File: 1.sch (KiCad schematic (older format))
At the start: 44 parts, among them J1 Micro_SD_Card, J10 I2C1, J11 I2C2, J12 B3..9A, J2 USB_B_Micro, J3 Conn_Power, J4 SWD, J5 Protected, J6 SPI1, J7 ADC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

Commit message: SD ground
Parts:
- J1: symbol Connector:Micro_SD_Card -> Connector:Micro_SD_Card_Det
- Y2: symbol Device:Crystal -> Device:Crystal_GND3
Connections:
- net GND: now also J1.10 (DET_A), J1.11 (SHIELD), Y2.3
- net OSC_32K1: now also Y2.1; no longer Y2.2
- net OSC_32K2: now also Y2.2; no longer Y2.1
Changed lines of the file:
@@
 Connection ~ 1000 2300
 Wire Wire Line
-	1000 2300 1000 2700
+	1000 2300 1000 2500
 Wire Wire Line
 	1250 2700 1000 2700
@@
 	1    8350 1250
 	1    0    0    -1
-$EndComp
-$Comp
-L Connector:Micro_SD_Card J1
-U 1 1 60953440
-P 1600 6700
-F 0 "J1" H 1550 7417 50  0000 C CNN
-F 1 "Micro_SD_Card" H 1550 7326 50  0000 C CNN
-F 2 "Connector_Card:microSD_HC_Hirose_DM3BT-DSF-PEJS" H 2750 7000 50  0001 C CNN
-F 3 "http://katalog.we-online.de/em/datasheet/693072010801.pdf" H 1600 6700 50  0001 C CNN
-	1    1600 6700
-	-1   0    0    -1
 $EndComp
 Wire Wire Line
@@
 Wire Wire Line
 	5450 2850 5550 2850
-Wire Wire Line
-	2600 6900 2600 7450
 Connection ~ 2600 7450
 Wire Wire Line
 	2600 7450 2600 7550
-Wire Wire Line
-	800  7300 800  7450
 Wire Wire Line
 	800  7450 2600 7450
@@
 	1750 2700 1900 2700
 $Comp
-L Device:Crystal Y2
-U 1 1 60880457
-P 1900 2500
-F 0 "Y2" V 1946 2369 50  0000 R CNN
-F 1 "32.768k" V 1855 2369 50  0000 R CNN
-F 2 "Crystal:Crystal_DS26_D2.0mm_L6.0mm_Horizontal_1EP_style1" H 1900 2500 50  0001 C CNN
-F 3 "~" H 1900 2500 50  0001 C CNN
-	1    1900 2500
-	0    -1   -1   0
-$EndComp
-$Comp
 L Connector_Generic:Conn_01x06 J10
 U 1 1 6153F296
@@
 	9300 1250 9200 1250
 Connection ~ 9200 1250
+$Comp
+L Connector:Micro_SD_Card_Det J1
+U 1 1 60953440
+P 1600 6800
+F 0 "J1" H 1550 7517 50  0000 C CNN
+F 1 "Micro_SD_Card" H 1550 7426 50  0000 C CNN
+F 2 "Connector_Card:microSD_HC_Hirose_DM3BT-DSF-PEJS" H 2750 7100 50  0001 C CNN
+F 3 "http://katalog.we-online.de/em/datasheet/693072010801.pdf" H 1600 6800 50  0001 C CNN
+	1    1600 6800
+	-1   0    0    -1
+$EndComp
+$Comp
+L Device:Crystal_GND3 Y2
+U 1 1 60880457
+P 1900 2500
+F 0 "Y2" V 1946 2369 50  0000 R CNN
+F 1 "32.768k" V 1855 2369 50  0000 R CNN
+F 2 "Crystal:Crystal_DS26_D2.0mm_L6.0mm_Horizontal_1EP_style1" H 1900 2500 50  0001 C CNN
+F 3 "~" H 1900 2500 50  0001 C CNN
+	1    1900 2500
+	0    1    1    0
+$EndComp
+Wire Wire Line
+	1700 2500 1000 2500
+Connection ~ 1000 2500
+Wire Wire Line
+	1000 2500 1000 2700
+Wire Wire Line
+	800  7300 800  7450
+Wire Wire Line
+	2600 6900 2600 7200
+Wire Wire Line
+	2500 7200 2600 7200
+Connection ~ 2600 7200
+Wire Wire Line
+	2600 7200 2600 7300
+Wire Wire Line
+	2500 7300 2600 7300
+Connection ~ 2600 7300
+Wire Wire Line
+	2600 7300 2600 7450
 $EndSCHEMATC

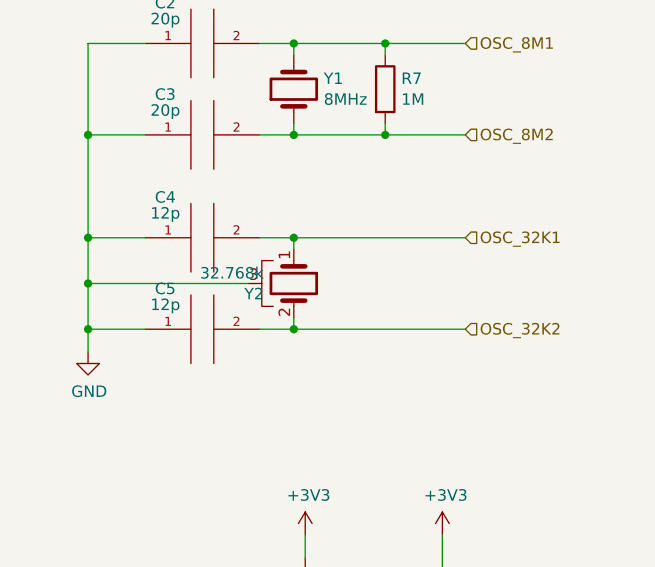
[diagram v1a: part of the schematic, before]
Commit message: fix: 32.768k OSC pin
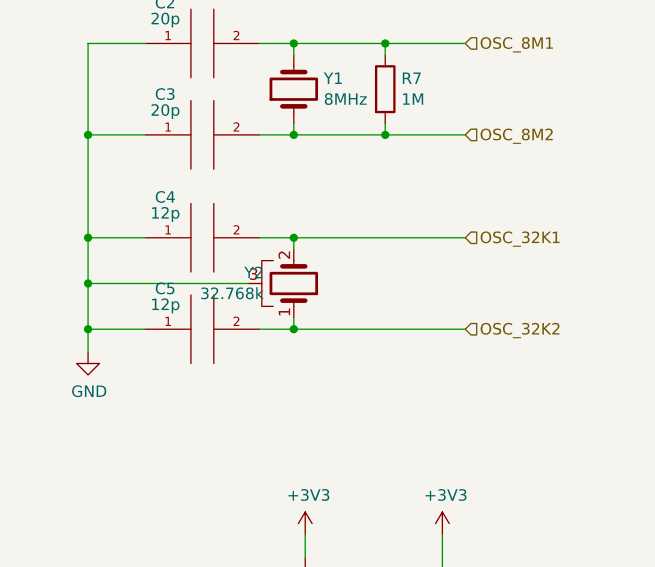
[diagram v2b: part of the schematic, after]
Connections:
- net OSC_32K1: now also Y2.2; no longer Y2.1
- net OSC_32K2: now also Y2.1; no longer Y2.2
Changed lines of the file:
@@
 	-1   0    0    -1
-$EndComp
-$Comp
-L Device:Crystal_GND3 Y2
-U 1 1 60880457
-P 1900 2500
-F 0 "Y2" V 1946 2369 50  0000 R CNN
-F 1 "32.768k" V 1855 2369 50  0000 R CNN
-F 2 "Crystal:Crystal_DS26_D2.0mm_L6.0mm_Horizontal_1EP_style1" H 1900 2500 50  0001 C CNN
-F 3 "~" H 1900 2500 50  0001 C CNN
-	1    1900 2500
-	0    1    1    0
 $EndComp
 Wire Wire Line
@@
 Wire Wire Line
 	2600 7300 2600 7450
+$Comp
+L Device:Crystal_GND3 Y2
+U 1 1 60880457
+P 1900 2500
+F 0 "Y2" V 1946 2369 50  0000 R CNN
+F 1 "32.768k" V 1855 2369 50  0000 R CNN
+F 2 "Crystal:Crystal_DS26_D2.0mm_L6.0mm_Horizontal_1EP_style1" H 1900 2500 50  0001 C CNN
+F 3 "~" H 1900 2500 50  0001 C CNN
+	1    1900 2500
+	0    1    -1   0
+$EndComp
 $EndSCHEMATC

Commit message: add 104 caps
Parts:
- added C11, C?: 104, Capacitor_SMD:C_0603_1608Metric, symbol Device:C_Small
- added C12: 104, Capacitor_SMD:C_0201_0603Metric, symbol Device:C_Small
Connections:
- net +3V3: now also C12.1, C?.1
- net GND: now also C11.2, C12.2, C?.2
- net at BT1.1 (+), U1.1 (VBAT): now also C11.1
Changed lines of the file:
@@
 L power:GND #PWR0128
 U 1 1 615BBC08
-P 4650 5050
-F 0 "#PWR0128" H 4650 4800 50  0001 C CNN
-F 1 "GND" H 4655 4877 50  0000 C CNN
-F 2 "" H 4650 5050 50  0001 C CNN
-F 3 "" H 4650 5050 50  0001 C CNN
-	1    4650 5050
+P 4650 5100
+F 0 "#PWR0128" H 4650 4850 50  0001 C CNN
+F 1 "GND" H 4655 4927 50  0000 C CNN
+F 2 "" H 4650 5100 50  0001 C CNN
+F 3 "" H 4650 5100 50  0001 C CNN
+	1    4650 5100
 	1    0    0    -1
 $EndComp
@@
 L power:GND #PWR0132
 U 1 1 616D0270
-P 4800 2850
-F 0 "#PWR0132" H 4800 2600 50  0001 C CNN
-F 1 "GND" H 4805 2677 50  0000 C CNN
-F 2 "" H 4800 2850 50  0001 C CNN
-F 3 "" H 4800 2850 50  0001 C CNN
-	1    4800 2850
-	1    0    0    -1
-$EndComp
-Wire Wire Line
-	4800 2800 4800 2850
+P 4400 2900
+F 0 "#PWR0132" H 4400 2650 50  0001 C CNN
+F 1 "GND" H 4405 2727 50  0000 C CNN
+F 2 "" H 4400 2900 50  0001 C CNN
+F 3 "" H 4400 2900 50  0001 C CNN
+	1    4400 2900
+	1    0    0    -1
+$EndComp
 Wire Wire Line
 	6050 2450 6050 2650
@@
 	1    0    0    -1
 $EndComp
-Wire Wire Line
-	4650 4850 4650 5050
 Text HLabel 4750 4950 2    50   Input ~ 0
 PB2
@@
 	0    1    -1   0
 $EndComp
+$Comp
+L Device:C_Small C11
+U 1 1 6096DC0F
+P 4400 2650
+F 0 "C11" H 4492 2696 50  0000 L CNN
+F 1 "104" H 4492 2605 50  0000 L CNN
+F 2 "Capacitor_SMD:C_0603_1608Metric" H 4400 2650 50  0001 C CNN
+F 3 "~" H 4400 2650 50  0001 C CNN
+	1    4400 2650
+	1    0    0    -1
+$EndComp
+Wire Wire Line
+	4400 2550 4400 2450
+Wire Wire Line
+	4400 2450 4800 2450
+Connection ~ 4800 2450
+Wire Wire Line
+	4400 2750 4400 2850
+Wire Wire Line
+	4800 2800 4800 2850
+Wire Wire Line
+	4800 2850 4400 2850
+Connection ~ 4400 2850
+Wire Wire Line
+	4400 2850 4400 2900
+$Comp
+L Device:C_Small C12
+U 1 1 609EBE25
+P 4800 4900
+F 0 "C12" H 4892 4946 50  0000 L CNN
+F 1 "104" H 4892 4855 50  0000 L CNN
+F 2 "Capacitor_SMD:C_0201_0603Metric" H 4800 4900 50  0001 C CNN
+F 3 "~" H 4800 4900 50  0001 C CNN
+	1    4800 4900
+	1    0    0    -1
+$EndComp
+Wire Wire Line
+	4800 4800 4800 4750
+Wire Wire Line
+	4800 4750 4700 4750
+Connection ~ 4700 4750
+Wire Wire Line
+	4650 4850 4650 5050
+Wire Wire Line
+	4800 5000 4800 5050
+Wire Wire Line
+	4800 5050 4650 5050
+Wire Wire Line
+	4650 5050 4650 5100
+Connection ~ 4650 5050
+$Comp
+L Device:C_Small C?
+U 1 1 60A78AA2
+P 6950 2850
+F 0 "C?" H 7042 2896 50  0000 L CNN
+F 1 "104" H 7042 2805 50  0000 L CNN
+F 2 "Capacitor_SMD:C_0603_1608Metric" H 6950 2850 50  0001 C CNN
+F 3 "~" H 6950 2850 50  0001 C CNN
+	1    6950 2850
+	1    0    0    -1
+$EndComp
+$Comp
+L power:GND #PWR?
+U 1 1 60A91FFF
+P 6950 3000
+F 0 "#PWR?" H 6950 2750 50  0001 C CNN
+F 1 "GND" H 6955 2827 50  0000 C CNN
+F 2 "" H 6950 3000 50  0001 C CNN
+F 3 "" H 6950 3000 50  0001 C CNN
+	1    6950 3000
+	1    0    0    -1
+$EndComp
+Wire Wire Line
+	6950 2950 6950 3000
+Wire Wire Line
+	6950 2600 6450 2600
+Wire Wire Line
+	6950 2600 6950 2750
+Connection ~ 6450 2600
 $EndSCHEMATC

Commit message: use 2x6 header for BxI2C1
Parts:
- removed J12: B3..9A, Connector_PinHeader_2.54mm:PinHeader_1x06_P2.54mm_Vertical, symbol Connector_Generic:Conn_01x06
- added J?: Conn_02x06_Odd_Even, symbol Connector_Generic:Conn_02x06_Odd_Even
- gave numbers to parts that had none: 1
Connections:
- net +3V3: now also J?.1 (Pin_1), J?.9 (Pin_9); no longer J10.1 (Pin_1), J10.5 (Pin_5)
- net GND: now also J?.11 (Pin_11), J?.3 (Pin_3); no longer J10.2 (Pin_2), J10.6 (Pin_6)
- net PA15: now also J?.2 (Pin_2)
- net PB3: now also J?.4 (Pin_4)
- net PB4: now also J?.6 (Pin_6)
- net PB5: now also J?.8 (Pin_8)
- net PB6: now also J?.5 (Pin_5); no longer J10.3 (Pin_3)
- net PB7: now also J?.7 (Pin_7); no longer J10.4 (Pin_4)
- net PB8: now also J?.10 (Pin_10)
- net PB9: now also J?.12 (Pin_12)
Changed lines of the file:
@@
 Wire Wire Line
 	2550 4450 2550 4500
-Text HLabel 2750 4500 2    50   Input ~ 0
-RG_LED
 Wire Wire Line
 	2750 4500 2550 4500
@@
 	10200 6200 10150 6200
 Wire Wire Line
-	3850 4950 3850 4850
+	3750 6050 3750 5950
 $Comp
 L power:GND #PWR0125
 U 1 1 61365714
-P 3850 4950
-F 0 "#PWR0125" H 3850 4700 50  0001 C CNN
-F 1 "GND" H 3855 4777 50  0000 C CNN
-F 2 "" H 3850 4950 50  0001 C CNN
-F 3 "" H 3850 4950 50  0001 C CNN
-	1    3850 4950
-	1    0    0    -1
-$EndComp
-Wire Wire Line
-	3800 4350 3800 4750
-Connection ~ 3850 4850
-Connection ~ 3800 4350
-Wire Wire Line
-	3800 4250 3800 4350
+P 3750 6050
+F 0 "#PWR0125" H 3750 5800 50  0001 C CNN
+F 1 "GND" H 3755 5877 50  0000 C CNN
+F 2 "" H 3750 6050 50  0001 C CNN
+F 3 "" H 3750 6050 50  0001 C CNN
+	1    3750 6050
+	1    0    0    -1
+$EndComp
+Wire Wire Line
+	3700 5450 3700 5850
+Connection ~ 3750 5950
+Connection ~ 3700 5450
+Wire Wire Line
+	3700 5350 3700 5450
 $Comp
 L power:+3V3 #PWR0126
 U 1 1 6130ED0C
-P 3800 4250
-F 0 "#PWR0126" H 3800 4100 50  0001 C CNN
-F 1 "+3V3" H 3815 4423 50  0000 C CNN
-F 2 "" H 3800 4250 50  0001 C CNN
-F 3 "" H 3800 4250 50  0001 C CNN
-	1    3800 4250
-	1    0    0    -1
-$EndComp
-Wire Wire Line
-	3850 4850 3900 4850
-Wire Wire Line
-	3800 4750 3900 4750
-Wire Wire Line
-	3900 4450 3850 4450
-Wire Wire Line
-	3800 4350 3900 4350
+P 3700 5350
+F 0 "#PWR0126" H 3700 5200 50  0001 C CNN
+F 1 "+3V3" H 3715 5523 50  0000 C CNN
+F 2 "" H 3700 5350 50  0001 C CNN
+F 3 "" H 3700 5350 50  0001 C CNN
+	1    3700 5350
+	1    0    0    -1
+$EndComp
 $Comp
 L Device:R R10
@@
 	10150 6200 10100 6200
 Wire Wire Line
-	3850 4450 3850 4850
-Text HLabel 3750 4550 0    50   Input ~ 0
+	3750 5550 3750 5950
+Text HLabel 3650 5650 0    50   Input ~ 0
 PB6
-Text HLabel 3750 4650 0    50   Input ~ 0
+Text HLabel 3650 5750 0    50   Input ~ 0
 PB7
-Wire Wire Line
-	3750 4550 3900 4550
-Wire Wire Line
-	3900 4650 3750 4650
 Text HLabel 4750 4650 2    50   Input ~ 0
 PB10
@@
 Wire Wire Line
 	6950 5450 6850 5450
-$Comp
-L Connector_Generic:Conn_01x06 J12
-U 1 1 617D7585
-P 8150 5850
-F 0 "J12" H 8230 5842 50  0000 L CNN
-F 1 "B3..9A" H 8230 5751 50  0000 L CNN
-F 2 "Connector_PinHeader_2.54mm:PinHeader_1x06_P2.54mm_Vertical" H 8150 5850 50  0001 C CNN
-F 3 "~" H 8150 5850 50  0001 C CNN
-	1    8150 5850
-	1    0    0    -1
-$EndComp
-Text HLabel 7850 5650 0    50   Input ~ 0
+Text HLabel 4450 5450 2    50   Input ~ 0
 PA15
-Wire Wire Line
-	7850 5650 7950 5650
-Text HLabel 7850 5750 0    50   Input ~ 0
+Text HLabel 4450 5550 2    50   Input ~ 0
 PB3
-Text HLabel 7850 5850 0    50   Input ~ 0
+Text HLabel 4450 5650 2    50   Input ~ 0
 PB4
-Text HLabel 7850 5950 0    50   Input ~ 0
+Text HLabel 4450 5750 2    50   Input ~ 0
 PB5
-Wire Wire Line
-	7850 5750 7950 5750
-Wire Wire Line
-	7950 5850 7850 5850
-Wire Wire Line
-	7850 5950 7950 5950
-Text HLabel 7850 6050 0    50   Input ~ 0
+Text HLabel 4450 5850 2    50   Input ~ 0
 PB8
-Text HLabel 7850 6150 0    50   Input ~ 0
+Text HLabel 4450 5950 2    50   Input ~ 0
 PB9
-Wire Wire Line
-	7850 6050 7950 6050
-Wire Wire Line
-	7950 6150 7850 6150
 Wire Wire Line
 	1900 2700 2650 2700
@@
 Connection ~ 4650 5050
 $Comp
-L Device:C_Small C?
+L Device:C_Small C13
 U 1 1 60A78AA2
 P 6950 2850
-F 0 "C?" H 7042 2896 50  0000 L CNN
+F 0 "C13" H 7042 2896 50  0000 L CNN
 F 1 "104" H 7042 2805 50  0000 L CNN
 F 2 "Capacitor_SMD:C_0603_1608Metric" H 6950 2850 50  0001 C CNN
@@
 $EndComp
 $Comp
-L power:GND #PWR?
+L power:GND #PWR0133
 U 1 1 60A91FFF
 P 6950 3000
-F 0 "#PWR?" H 6950 2750 50  0001 C CNN
+F 0 "#PWR0133" H 6950 2750 50  0001 C CNN
 F 1 "GND" H 6955 2827 50  0000 C CNN
 F 2 "" H 6950 3000 50  0001 C CNN
@@
 	6950 2600 6950 2750
 Connection ~ 6450 2600
+$Comp
+L Connector_Generic:Conn_02x06_Odd_Even J?
+U 1 1 60B34FEB
+P 4050 5650
+F 0 "J?" H 4100 6067 50  0000 C CNN
+F 1 "Conn_02x06_Odd_Even" H 4100 5976 50  0000 C CNN
+F 2 "" H 4050 5650 50  0001 C CNN
+F 3 "~" H 4050 5650 50  0001 C CNN
+	1    4050 5650
+	1    0    0    -1
+$EndComp
+Text HLabel 2750 4500 2    50   Input ~ 0
+RG_LED
+Wire Wire Line
+	4450 5450 4350 5450
+Wire Wire Line
+	4350 5550 4450 5550
+Wire Wire Line
+	4450 5650 4350 5650
+Wire Wire Line
+	4350 5750 4450 5750
+Wire Wire Line
+	4450 5850 4350 5850
+Wire Wire Line
+	4350 5950 4450 5950
+Wire Wire Line
+	3700 5450 3850 5450
+Wire Wire Line
+	3750 5550 3850 5550
+Wire Wire Line
+	3650 5650 3850 5650
+Wire Wire Line
+	3650 5750 3850 5750
+Wire Wire Line
+	3700 5850 3850 5850
+Wire Wire Line
+	3750 5950 3850 5950
 $EndSCHEMATC

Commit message: abc123
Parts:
- removed J10: I2C1, Connector_PinHeader_2.54mm:PinHeader_1x06_P2.54mm_Vertical, symbol Connector_Generic:Conn_01x06
- J10: renamed from J?; value Conn_02x06_Odd_Even -> BxI2C1; footprint (none) -> Connector_PinHeader_2.54mm:PinHeader_2x06_P2.54mm_Vertical
- J3: value Conn_Power -> Power
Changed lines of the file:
@@
 P 10500 1450
 F 0 "J3" H 10550 1867 50  0000 C CNN
-F 1 "Conn_Power" H 10550 1776 50  0000 C CNN
+F 1 "Power" H 10550 1776 50  0000 C CNN
 F 2 "Connector_PinHeader_2.54mm:PinHeader_2x06_P2.54mm_Vertical" H 10500 1450 50  0001 C CNN
 F 3 "~" H 10500 1450 50  0001 C CNN
@@
 Wire Wire Line
 	1750 2700 1900 2700
-$Comp
-L Connector_Generic:Conn_01x06 J10
-U 1 1 6153F296
-P 4100 4550
-F 0 "J10" H 4055 4961 50  0000 L CNN
-F 1 "I2C1" H 4134 4921 50  0000 C TNN
-F 2 "Connector_PinHeader_2.54mm:PinHeader_1x06_P2.54mm_Vertical" H 4100 4550 50  0001 C CNN
-F 3 "~" H 4100 4550 50  0001 C CNN
-	1    4100 4550
-	1    0    0    -1
-$EndComp
 Text HLabel 4750 4950 2    50   Input ~ 0
 PB2
@@
 Connection ~ 6450 2600
 $Comp
-L Connector_Generic:Conn_02x06_Odd_Even J?
+L Connector_Generic:Conn_02x06_Odd_Even J10
 U 1 1 60B34FEB
 P 4050 5650
-F 0 "J?" H 4100 6067 50  0000 C CNN
-F 1 "Conn_02x06_Odd_Even" H 4100 5976 50  0000 C CNN
-F 2 "" H 4050 5650 50  0001 C CNN
+F 0 "J10" H 4100 6067 50  0000 C CNN
+F 1 "BxI2C1" H 4100 5976 50  0000 C CNN
+F 2 "Connector_PinHeader_2.54mm:PinHeader_2x06_P2.54mm_Vertical" H 4050 5650 50  0001 C CNN
 F 3 "~" H 4050 5650 50  0001 C CNN
 	1    4050 5650
